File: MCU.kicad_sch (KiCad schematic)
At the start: 29 parts, among them J10 Conn_01x04, J11 Conn_01x03, J6 Conn_01x04, J7 Conn_ST_STDC14, J8 Conn_01x03, J9 Conn_01x04, U16 STM32F303RETx

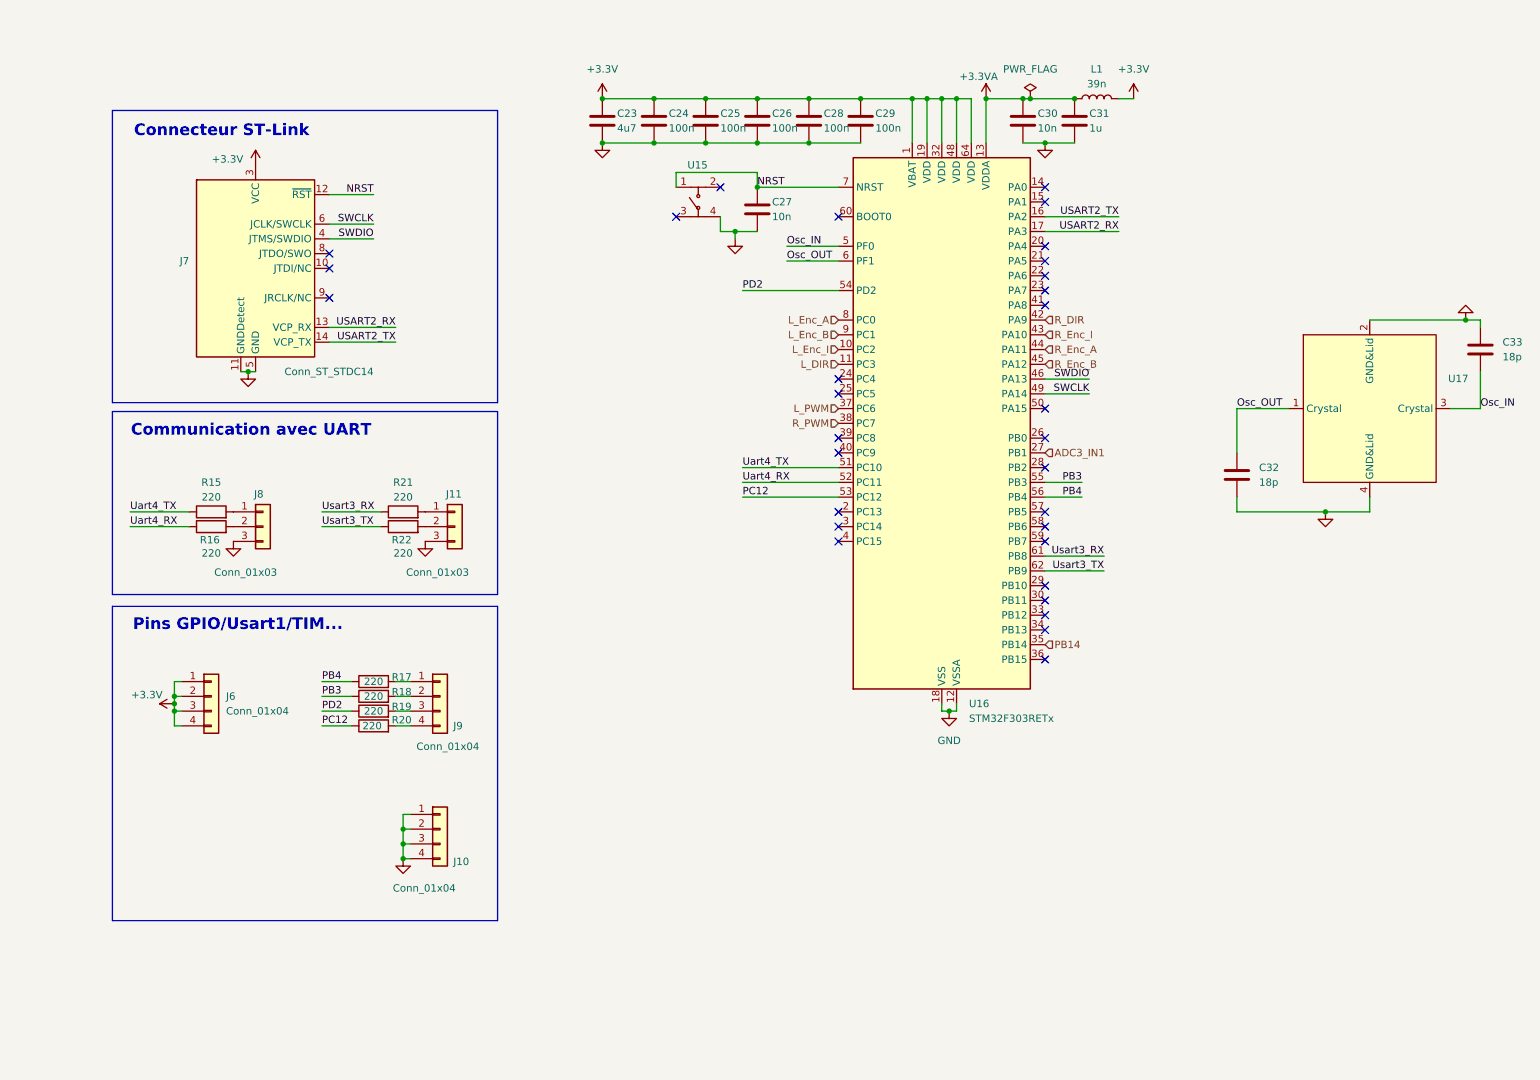
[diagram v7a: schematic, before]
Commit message: V2 Driver-- avec control de courant
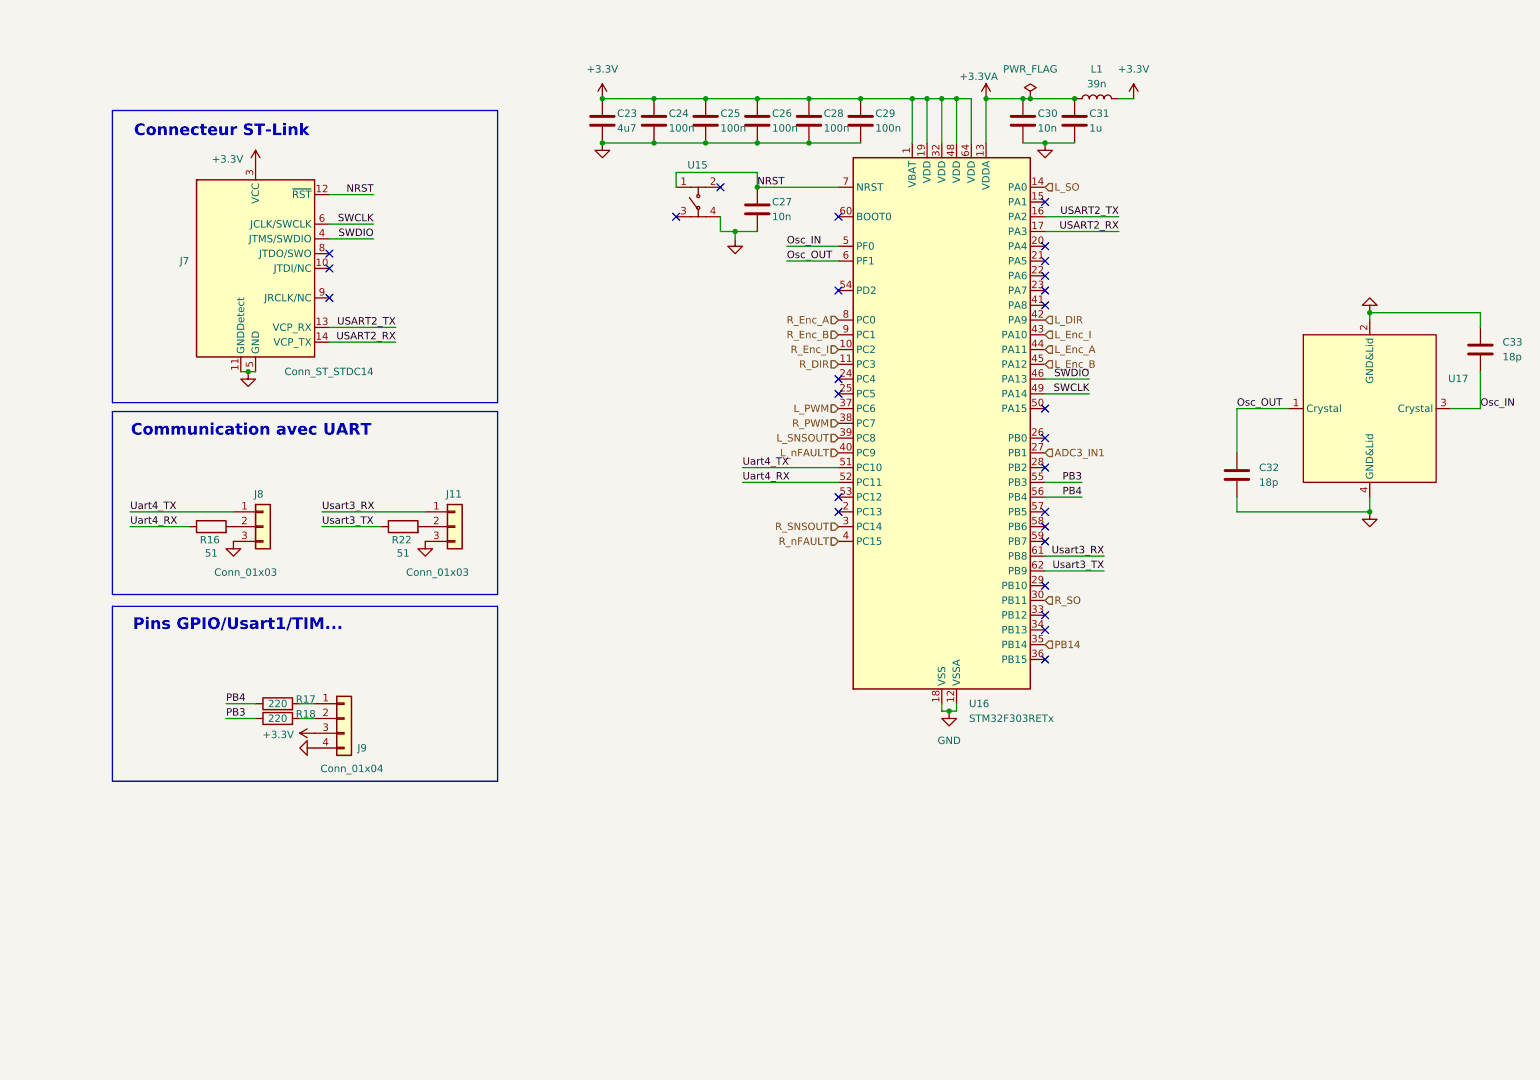
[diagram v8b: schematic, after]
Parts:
- removed J10, J6: Conn_01x04, Connector_PinHeader_2.54mm:PinHeader_1x04_P2.54mm_Vertical, symbol Connector_Generic:Conn_01x04
- removed R15, R19, R20, R21: 220, Resistor_SMD:R_0402_1005Metric, symbol Device:R
- J11, J8: footprint Connector_JST:JST_PH_B3B-PH-K_1x03_P2.00mm_Vertical -> Connector_JST:JST_EH_B3B-EH-A_1x03_P2.50mm_Vertical
- R16, R22: value 220 -> 51
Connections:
- net +3.3V: now also J9.3 (Pin_3)
- net GND: now also J9.4 (Pin_4)
- net L_DIR: now also U16.42 (PA9); no longer U16.11 (PC3)
- net L_Enc_A: now also U16.44 (PA11); no longer U16.8 (PC0)
- net L_Enc_B: now also U16.45 (PA12); no longer U16.9 (PC1)
- net L_Enc_I: now also U16.43 (PA10); no longer U16.10 (PC2)
- net R_DIR: now also U16.11 (PC3); no longer U16.42 (PA9)
- net R_Enc_A: now also U16.8 (PC0); no longer U16.44 (PA11)
- net R_Enc_B: now also U16.9 (PC1); no longer U16.45 (PA12)
- net R_Enc_I: now also U16.10 (PC2); no longer U16.43 (PA10)
- net USART2_RX: now also J7.14 (VCP_TX); no longer J7.13 (VCP_RX)
- net USART2_TX: now also J7.13 (VCP_RX); no longer J7.14 (VCP_TX)
- net Uart4_TX: now also J8.1 (Pin_1)
- net Usart3_RX: now also J11.1 (Pin_1)
- net L_SO: now reaches U16.14 (PA0)
- net R_SNSOUT: now reaches U16.3 (PC14)
- net R_SO: now reaches U16.30 (PB11)
- net L_SNSOUT: now reaches U16.39 (PC8)
- net R_nFAULT: now reaches U16.4 (PC15)
- net L_nFAULT: now reaches U16.40 (PC9)
- net PC12: no longer names the net of U16.53 (PC12)
- net PD2: no longer names the net of U16.54 (PD2)
- no-connect marks 31 -> 27
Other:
- moved on the sheet: J9, R17, R18
